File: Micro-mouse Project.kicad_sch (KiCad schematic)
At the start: 10 parts, among them U1 DRV8833PWPR

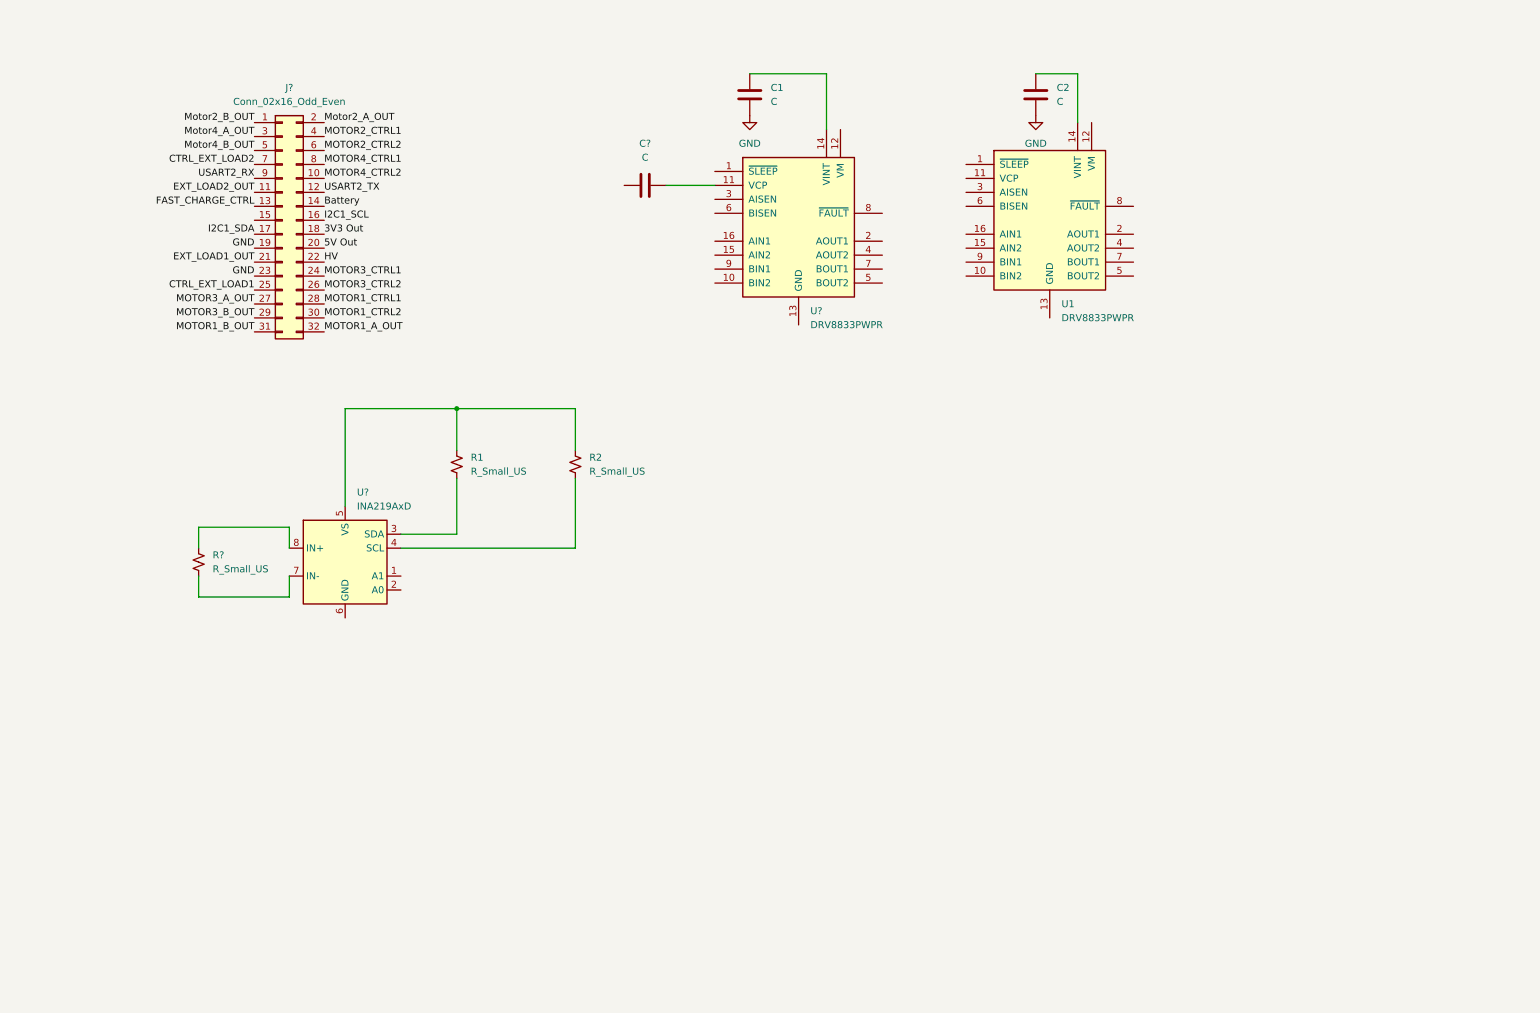
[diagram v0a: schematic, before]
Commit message: Complete Motor Management
Made sure all power flags are included.
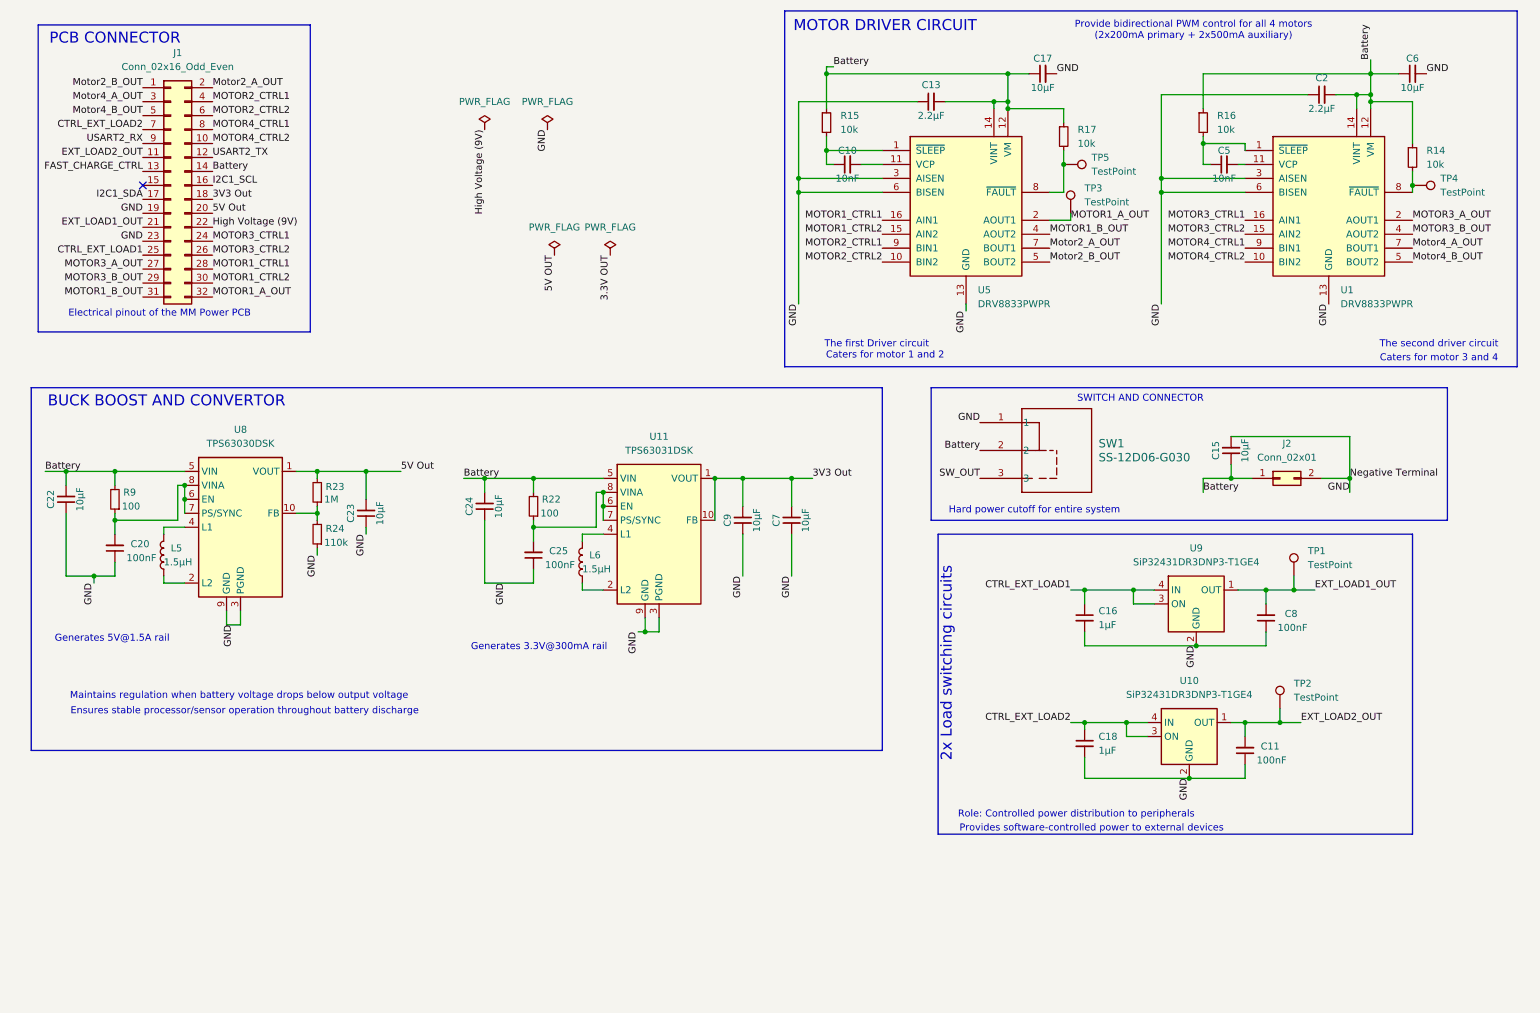
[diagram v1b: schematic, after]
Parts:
- removed C1, C2, C?: C, symbol Device:C
- removed R1, R2, R?: R_Small_US, symbol Device:R_Small_US
- removed U?: INA219AxD, Package_SO:SOIC-8_3.9x4.9mm_P1.27mm, symbol Sensor_Energy:INA219AxD
- added C10, C5: 10nF, Capacitor_SMD:C_0805_2012Metric_Pad1.18x1.45mm_HandSolder, symbol Device:C_Small
- added C11, C20, C25, C8: 100nF, Capacitor_SMD:C_0402_1005Metric_Pad0.74x0.62mm_HandSolder, symbol Device:C_Small
- added C13, C2: 2.2μF, Capacitor_SMD:C_0402_1005Metric_Pad0.74x0.62mm_HandSolder, symbol Device:C_Small
- added C15, C17, C22, C23, C24, C6, C7, C9: 10μF, Capacitor_SMD:C_1206_3216Metric_Pad1.33x1.80mm_HandSolder, symbol Device:C_Small
- added C16, C18: 1μF, Capacitor_SMD:C_1206_3216Metric_Pad1.33x1.80mm_HandSolder, symbol Device:C_Small
- added J2: Conn_02x01, symbol Connector_Generic:Conn_02x01
- added L5, L6: 1.5µH, Inductor_SMD:L_1206_3216Metric_Pad1.22x1.90mm_HandSolder, symbol Device:L
- added R14, R15, R16, R17: 10k, Resistor_SMD:R_0805_2012Metric_Pad1.20x1.40mm_HandSolder, symbol Device:R_Small
- added R22, R9: 100, Resistor_SMD:R_0805_2012Metric_Pad1.20x1.40mm_HandSolder, symbol Device:R_Small
- added R23: 1M, Resistor_SMD:R_1206_3216Metric_Pad1.30x1.75mm_HandSolder, symbol Device:R_Small
- added R24: 110k, Resistor_SMD:R_0805_2012Metric_Pad1.20x1.40mm_HandSolder, symbol Device:R_Small
- added SW1: SS-12D06-G030, Library:SS-12D06_GSW, symbol 2025-03-28_06-57-30:SS-12D06-G030
- added TP1, TP2, TP3, TP4, TP5: TestPoint, symbol Connector:TestPoint
- added U10: SiP32431DR3DNP3-T1GE4, Library:SON50P120X160X60-5N, symbol Power_Management:SiP32431DR3
- added U11: TPS63031DSK, Package_SON:WSON-10-1EP_2.5x2.5mm_P0.5mm_EP1.2x2mm, symbol Regulator_Switching:TPS63031DSK
- added U8: TPS63030DSK, Package_SON:WSON-10-1EP_2.5x2.5mm_P0.5mm_EP1.2x2mm, symbol Regulator_Switching:TPS63030DSK
- added U9: SiP32431DR3DNP3-T1GE4, Package_TO_SOT_SMD:SOT-363_SC-70-6, symbol Power_Management:SiP32431DR3
- U1: footprint Package_SO:HTSSOP-16-1EP_4.4x5mm_P0.65mm_EP3.4x5mm_Mask2.46x2.31mm_ThermalVias -> Library:IC_DRV8833PWPR
- U5: renamed from U?; footprint Package_SO:HTSSOP-16-1EP_4.4x5mm_P0.65mm_EP3.4x5mm_Mask2.46x2.31mm_ThermalVias -> Library:IC_DRV8833PWPR
- gave numbers to parts that had none: 1
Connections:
- net 3V3 Out: now also C7.2, C9.2, U11.1 (VOUT), U11.10 (FB)
- net 5V Out: now also C23.2, R23.2, U8.1 (VOUT)
- net Battery: now also U1.12 (VM), U1.14 (VINT), U5.12 (VM), U5.14 (VINT), C13.2, C15.1, C17.1, C2.2, C22.2, C24.2, C6.1, J2.1 (Pin_1), R14.1, R15.1, R16.1, R17.1, R22.2, R9.2, SW1.2, U11.5 (VIN), U8.5 (VIN)
- net CTRL_EXT_LOAD1: now also C16.1, U9.3 (ON), U9.4 (IN)
- net CTRL_EXT_LOAD2: now also C18.1, U10.3 (ON), U10.4 (IN)
- net EXT_LOAD1_OUT: now also C8.2, TP1.1, U9.1 (OUT)
- net EXT_LOAD2_OUT: now also C11.2, TP2.1, U10.1 (OUT)
- net GND: now also U1.13 (GND), U1.17 (GND), U1.3 (AISEN), U1.6 (BISEN), U5.13 (GND), U5.17 (GND), U5.3 (AISEN), U5.6 (BISEN), C11.1, C13.1, C15.2, C16.2, C17.2, C18.2, C2.1, C20.1, C22.1, C23.1, C24.1, C25.1, C6.2, C7.1, C8.1, C9.1, J2.2 (Pin_2), R24.1, SW1.1, U10.2 (GND), U10.5 (GND), U11.11 (PGND), U11.3 (PGND), U11.9 (GND), U8.11 (PGND), U8.3 (PGND), U8.9 (GND), U9.2 (GND), U9.5 (GND)
- net MOTOR1_A_OUT: now also U5.2 (AOUT1), TP3.1
- net MOTOR1_B_OUT: now also U5.4 (AOUT2)
- net MOTOR1_CTRL1: now also U5.16 (AIN1)
- net MOTOR1_CTRL2: now also U5.15 (AIN2)
- net MOTOR2_CTRL1: now also U5.9 (BIN1)
- net MOTOR2_CTRL2: now also U5.10 (BIN2)
- net MOTOR3_A_OUT: now also U1.2 (AOUT1)
- net MOTOR3_B_OUT: now also U1.4 (AOUT2)
- net MOTOR3_CTRL1: now also U1.16 (AIN1)
- net MOTOR3_CTRL2: now also U1.15 (AIN2)
- net MOTOR4_CTRL1: now also U1.9 (BIN1)
- net MOTOR4_CTRL2: now also U1.10 (BIN2)
- net Motor2_A_OUT: now also U5.7 (BOUT1)
- net Motor2_B_OUT: now also U5.5 (BOUT2)
- net Motor4_A_OUT: now also U1.7 (BOUT1)
- net Motor4_B_OUT: now also U1.5 (BOUT2)
- net at U1.1 (~{SLEEP}): now also C5.1, R16.2
- net at U1.11 (VCP): now also C5.2
- net at U1.8 (~{FAULT}): now also R14.2, TP4.1
- net at U5.1 (~{SLEEP}): now also C10.1, R15.2
- net at U5.11 (VCP): now also C10.2
- net at U5.8 (~{FAULT}): now also R17.2, TP5.1
- net HV renamed High Voltage (9V)
- new net: C20.2, R9.1, U8.6 (EN), U8.7 (PS/SYNC), U8.8 (VINA)
- new net: R23.1, R24.2, U8.10 (FB)
- new net: L6.1, U11.2 (L2)
- new net: L6.2, U11.4 (L1)
- new net: L5.1, U8.2 (L2)
- new net: L5.2, U8.4 (L1)
- new net: C25.2, R22.1, U11.6 (EN), U11.7 (PS/SYNC), U11.8 (VINA)
- new net SW_OUT: SW1.3
- no-connect marks 0 -> 1
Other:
- note added: "2x Load switching circuits"
- note added: "BUCK BOOST AND CONVERTOR"
- note added: "Caters for motor 1 and 2"
- note added: "Caters for motor 3 and 4"
- note added: "Electrical pinout of the MM Power PCB"
- note added: "Ensures stable processor/sensor operation throughout battery discharge"
- note added: "Generates 3.3V@300mA rail"
- note added: "Generates 5V@1.5A rail"
- note added: "Hard power cutoff for entire system"
- note added: "MOTOR DRIVER CIRCUIT"
- note added: "Maintains regulation when battery voltage drops below output voltage"
- note added: "PCB CONNECTOR"
- note added: "Provide bidirectional PWM control for all 4 motors (2x200mA primary + 2x500mA auxiliary)"
- note added: "Provides software-controlled power to external devices"
- note added: "Role: Controlled power distribution to peripherals"
- note added: "SWITCH AND CONNECTOR"
- note added: "The first Driver circuit"
- note added: "The second driver circuit"
- company: (none) -> Universiy of Cape Town
- title: (none) -> GRP 14 POWER SUB-SYSTEM
- moved on the sheet: J1, U1, U5

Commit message: Revert "Complete Motor Management"
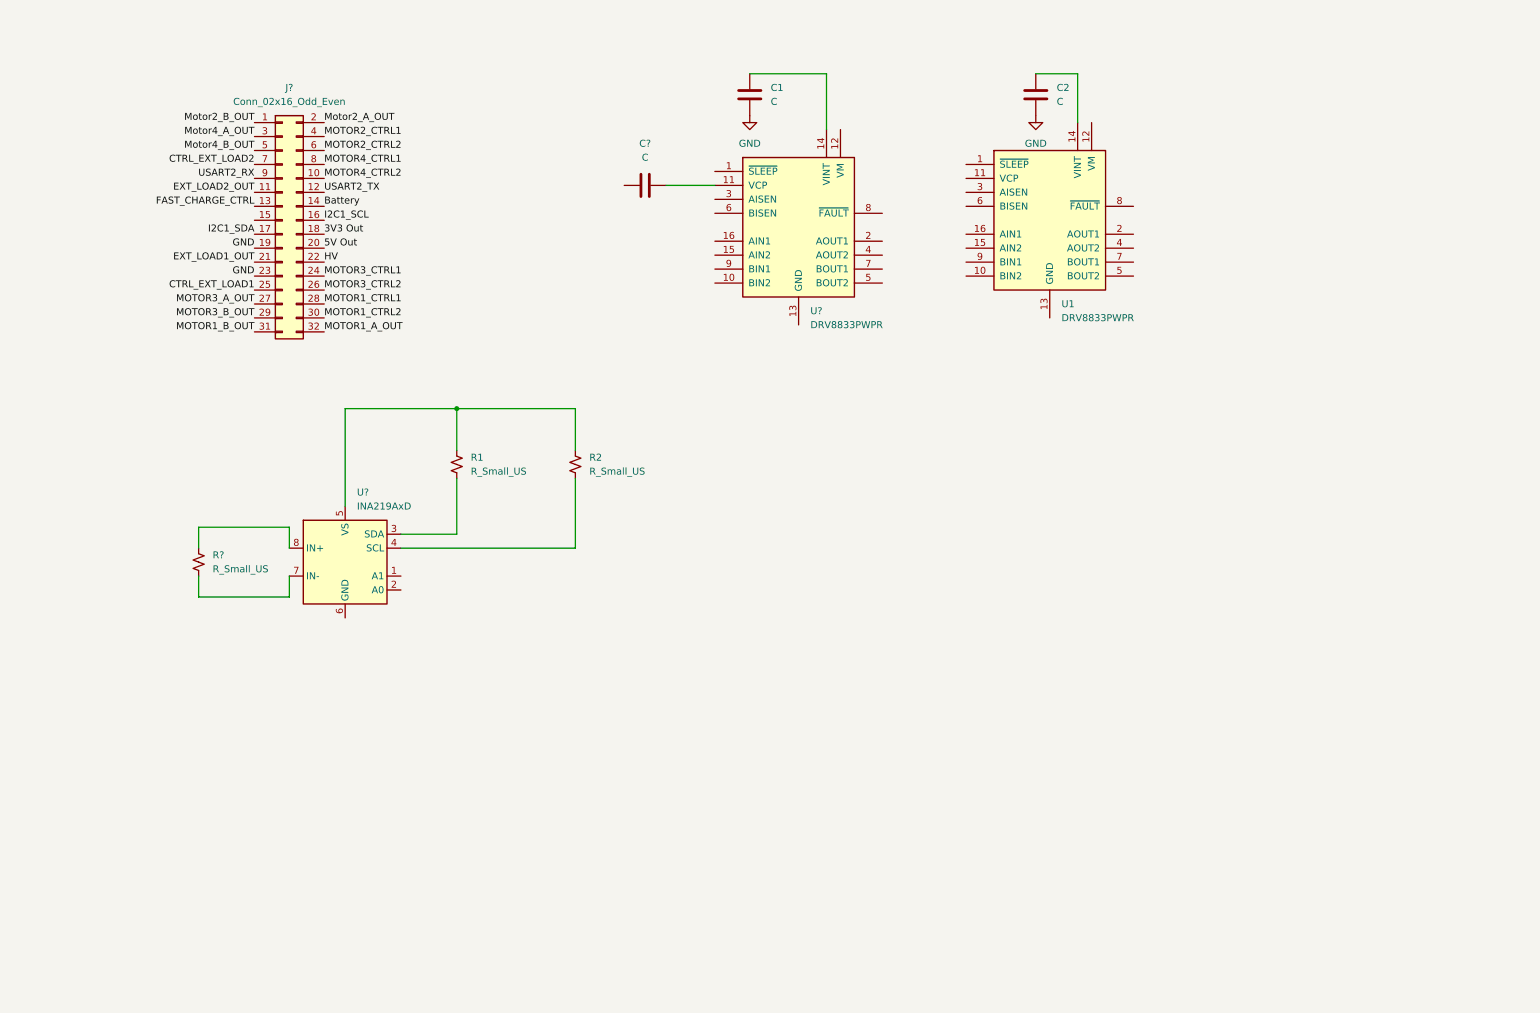
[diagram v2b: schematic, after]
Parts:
- removed C10, C5: 10nF, Capacitor_SMD:C_0805_2012Metric_Pad1.18x1.45mm_HandSolder, symbol Device:C_Small
- removed C11, C20, C25, C8: 100nF, Capacitor_SMD:C_0402_1005Metric_Pad0.74x0.62mm_HandSolder, symbol Device:C_Small
- removed C13, C2: 2.2μF, Capacitor_SMD:C_0402_1005Metric_Pad0.74x0.62mm_HandSolder, symbol Device:C_Small
- removed C15, C17, C22, C23, C24, C6, C7, C9: 10μF, Capacitor_SMD:C_1206_3216Metric_Pad1.33x1.80mm_HandSolder, symbol Device:C_Small
- removed C16, C18: 1μF, Capacitor_SMD:C_1206_3216Metric_Pad1.33x1.80mm_HandSolder, symbol Device:C_Small
- removed J2: Conn_02x01, symbol Connector_Generic:Conn_02x01
- removed L5, L6: 1.5µH, Inductor_SMD:L_1206_3216Metric_Pad1.22x1.90mm_HandSolder, symbol Device:L
- removed R14, R15, R16, R17: 10k, Resistor_SMD:R_0805_2012Metric_Pad1.20x1.40mm_HandSolder, symbol Device:R_Small
- removed R22, R9: 100, Resistor_SMD:R_0805_2012Metric_Pad1.20x1.40mm_HandSolder, symbol Device:R_Small
- removed R23: 1M, Resistor_SMD:R_1206_3216Metric_Pad1.30x1.75mm_HandSolder, symbol Device:R_Small
- removed R24: 110k, Resistor_SMD:R_0805_2012Metric_Pad1.20x1.40mm_HandSolder, symbol Device:R_Small
- removed SW1: SS-12D06-G030, Library:SS-12D06_GSW, symbol 2025-03-28_06-57-30:SS-12D06-G030
- removed TP1, TP2, TP3, TP4, TP5: TestPoint, symbol Connector:TestPoint
- removed U10: SiP32431DR3DNP3-T1GE4, Library:SON50P120X160X60-5N, symbol Power_Management:SiP32431DR3
- removed U11: TPS63031DSK, Package_SON:WSON-10-1EP_2.5x2.5mm_P0.5mm_EP1.2x2mm, symbol Regulator_Switching:TPS63031DSK
- removed U8: TPS63030DSK, Package_SON:WSON-10-1EP_2.5x2.5mm_P0.5mm_EP1.2x2mm, symbol Regulator_Switching:TPS63030DSK
- removed U9: SiP32431DR3DNP3-T1GE4, Package_TO_SOT_SMD:SOT-363_SC-70-6, symbol Power_Management:SiP32431DR3
- added C1, C2, C?: C, symbol Device:C
- added R1, R2, R?: R_Small_US, symbol Device:R_Small_US
- added U?: INA219AxD, Package_SO:SOIC-8_3.9x4.9mm_P1.27mm, symbol Sensor_Energy:INA219AxD
- U1: footprint Library:IC_DRV8833PWPR -> Package_SO:HTSSOP-16-1EP_4.4x5mm_P0.65mm_EP3.4x5mm_Mask2.46x2.31mm_ThermalVias
- U?: renamed from U5; footprint Library:IC_DRV8833PWPR -> Package_SO:HTSSOP-16-1EP_4.4x5mm_P0.65mm_EP3.4x5mm_Mask2.46x2.31mm_ThermalVias
- renumbered J1 to J?
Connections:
- net Battery: no longer U1.12 (VM), U1.14 (VINT), U?.12 (VM), U?.14 (VINT)
- net GND: now also C1.1, C2.1; no longer U1.13 (GND), U1.17 (GND), U1.3 (AISEN), U1.6 (BISEN), U?.13 (GND), U?.17 (GND), U?.3 (AISEN), U?.6 (BISEN)
- net MOTOR1_A_OUT: no longer U?.2 (AOUT1)
- net MOTOR1_B_OUT: no longer U?.4 (AOUT2)
- net MOTOR1_CTRL1: no longer U?.16 (AIN1)
- net MOTOR1_CTRL2: no longer U?.15 (AIN2)
- net MOTOR2_CTRL1: no longer U?.9 (BIN1)
- net MOTOR2_CTRL2: no longer U?.10 (BIN2)
- net MOTOR3_A_OUT: no longer U1.2 (AOUT1)
- net MOTOR3_B_OUT: no longer U1.4 (AOUT2)
- net MOTOR3_CTRL1: no longer U1.16 (AIN1)
- net MOTOR3_CTRL2: no longer U1.15 (AIN2)
- net MOTOR4_CTRL1: no longer U1.9 (BIN1)
- net MOTOR4_CTRL2: no longer U1.10 (BIN2)
- net Motor2_A_OUT: no longer U?.7 (BOUT1)
- net Motor2_B_OUT: no longer U?.5 (BOUT2)
- net Motor4_A_OUT: no longer U1.7 (BOUT1)
- net Motor4_B_OUT: no longer U1.5 (BOUT2)
- net at U?.11 (VCP): now also C?.2
- net High Voltage (9V) renamed HV
- new net: R2.1, U?.4 (SCL)
- new net: R1.2, R2.2, U?.5 (VS)
- new net: U1.13 (GND), U1.17 (GND)
- new net: C2.2, U1.14 (VINT)
- new net: R1.1, U?.3 (SDA)
- new net: R?.1, U?.7 (IN-)
- new net: R?.2, U?.8 (IN+)
- new net: U?.13 (GND), U?.17 (GND)
- new net: C1.2, U?.14 (VINT)
- no-connect marks 1 -> 0
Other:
- note removed: "2x Load switching circuits"
- note removed: "BUCK BOOST AND CONVERTOR"
- note removed: "Caters for motor 1 and 2"
- note removed: "Caters for motor 3 and 4"
- note removed: "Electrical pinout of the MM Power PCB"
- note removed: "Ensures stable processor/sensor operation throughout battery discharge"
- note removed: "Generates 3.3V@300mA rail"
- note removed: "Generates 5V@1.5A rail"
- note removed: "Hard power cutoff for entire system"
- note removed: "MOTOR DRIVER CIRCUIT"
- note removed: "Maintains regulation when battery voltage drops below output voltage"
- note removed: "PCB CONNECTOR"
- note removed: "Provide bidirectional PWM control for all 4 motors (2x200mA primary + 2x500mA auxiliary)"
- note removed: "Provides software-controlled power to external devices"
- note removed: "Role: Controlled power distribution to peripherals"
- note removed: "SWITCH AND CONNECTOR"
- note removed: "The first Driver circuit"
- note removed: "The second driver circuit"
- company: Universiy of Cape Town -> (none)
- title: GRP 14 POWER SUB-SYSTEM -> (none)
- moved on the sheet: J?, U1, U?
